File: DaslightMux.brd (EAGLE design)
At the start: 60 x 55.9 mm, 11 parts, among them U1 XC9572XL

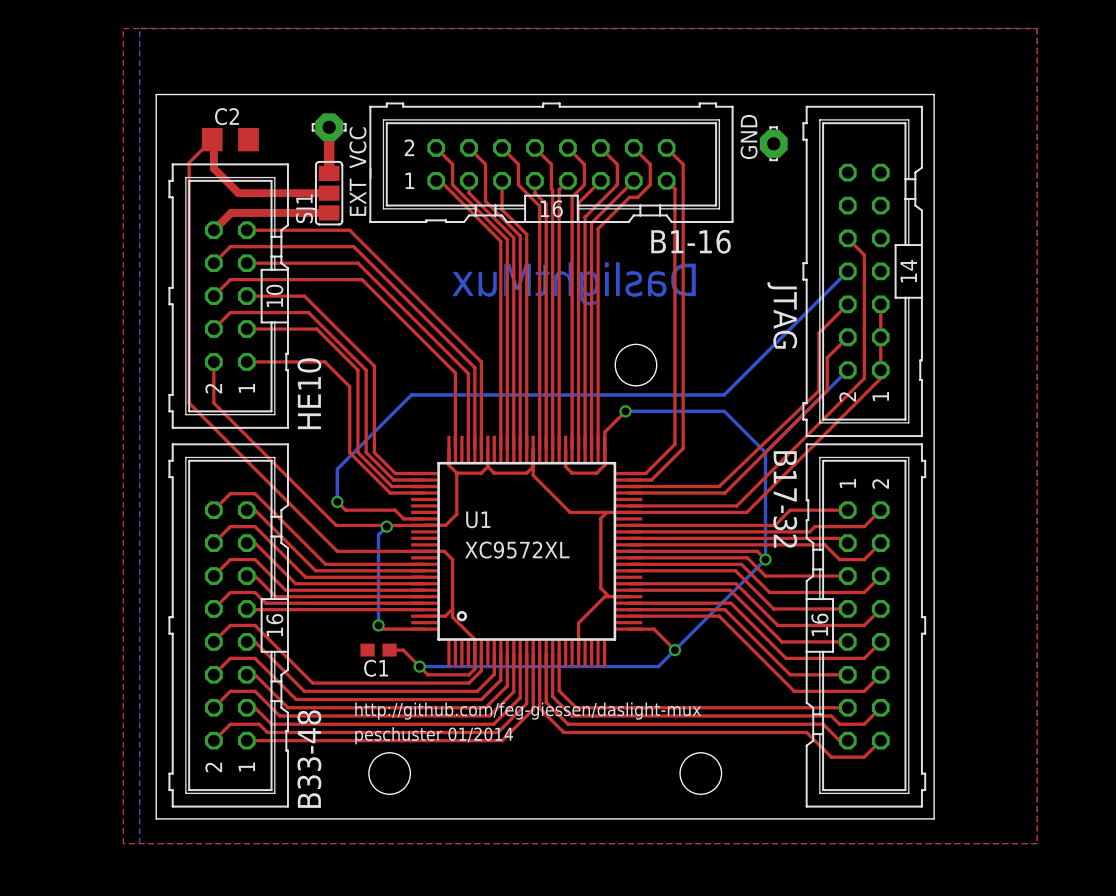
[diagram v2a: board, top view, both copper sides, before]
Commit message: Changed to SUB-D, therefore swapped "all" pins
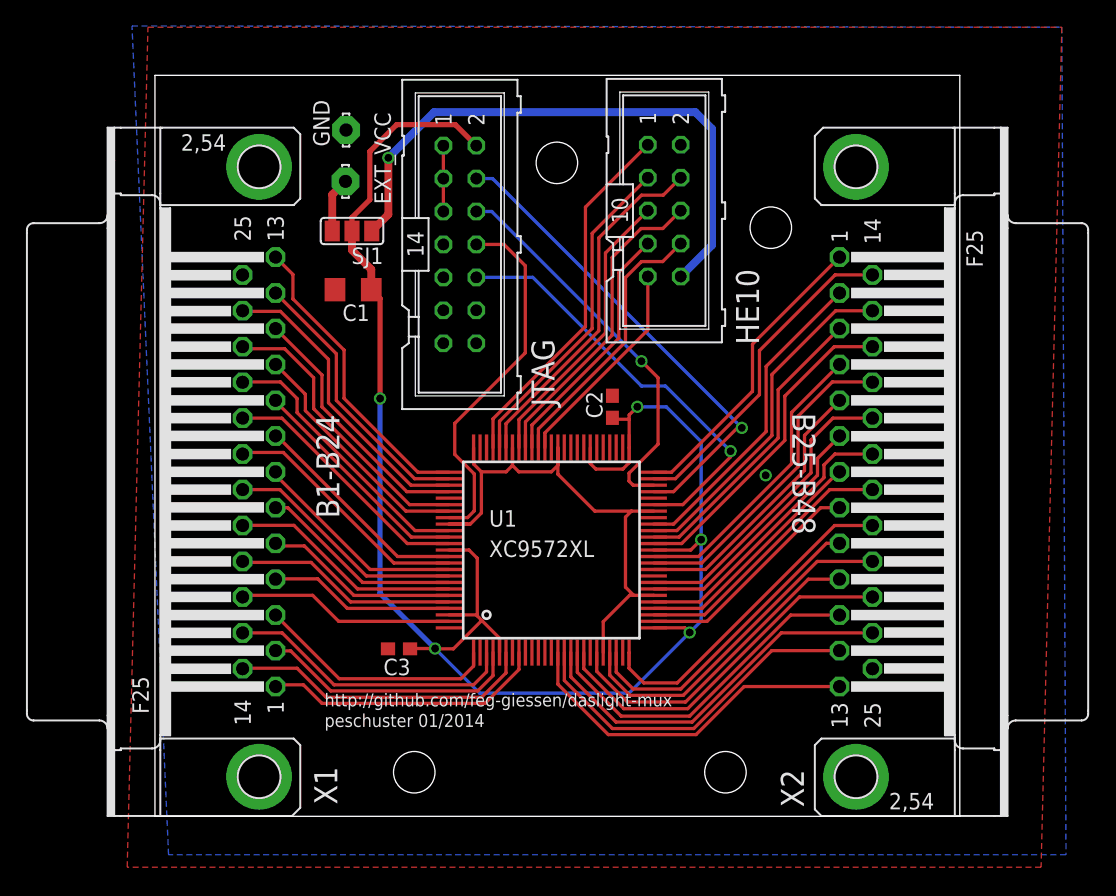
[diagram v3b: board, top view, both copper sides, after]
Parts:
- removed SV3: B1-16, con-harting-ml:ML16
- removed SV4: B17-32, con-harting-ml:ML16
- removed SV5: B33-48, con-harting-ml:ML16
- added C3: 100n, resistor:C0603
- added X1: B1-B24, con-subd:F25HP
- added X2: B25-B48, con-subd:F25HP
- C1: value 100n -> 10u; device resistor:C0603 -> resistor:C1206
- C2: value 10u -> 100n; device resistor:C1206 -> resistor:C0603
- SJ1: value (none) -> PWR_SEL
- moved C2 36.0 mm to (35.2, 31.8), turned to 90 degrees
- moved SV2 34.1 mm to (39.2, 46.9), turned to 270 degrees
- moved GND 33.0 mm to (14.6, 53.1)
- moved SV1 31.3 mm to (23.4, 44.3), turned to 270 degrees
- moved C1 27.9 mm to (15.2, 40.8)
- moved EXT_VCC 4.35 mm to (14.6, 49.2), turned to 270 degrees
- moved SJ1 3.41 mm to (15.1, 45.3), turned to 180 degrees
- moved U1 1.90 mm to (30.5, 20.7)
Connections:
- net B1: now also U1.8, X1.1; no longer SV3.1, U1.67
- net B10: now also U1.82, X1.10; no longer SV3.10, U1.56
- net B11: now also U1.79, X1.11; no longer SV3.11, U1.55
- net B12: now also U1.77, X1.12; no longer SV3.12, U1.54
- net B13: now also U1.76, X1.13; no longer SV3.13, U1.53
- net B14: now also U1.6, X1.14; no longer SV3.14, U1.52
- net B15: now also U1.3, X1.15; no longer SV3.15, U1.50
- net B16: now also U1.99, X1.16; no longer SV3.16, U1.49
- net B17: now also U1.96, X1.17; no longer SV4.1, U1.42
- net B18: now also U1.94, X1.18; no longer SV4.2, U1.41
- net B19: now also U1.92, X1.19; no longer SV4.3, U1.40
- net B2: now also U1.4, X1.2; no longer SV3.2, U1.66
- net B20: now also U1.90, X1.20; no longer SV4.4, U1.39
- net B21: now also U1.87, X1.21; no longer SV4.5, U1.37
- net B22: now also U1.85, X1.22; no longer SV4.6, U1.36
- net B23: now also U1.81, X1.23; no longer SV4.7, U1.35
- net B24: now also U1.78, X1.24; no longer SV4.8, U1.33
- net B25: now also U1.50, X2.1; no longer SV4.9, U1.32
- net B26: now also U1.42, X2.2; no longer SV4.10, U1.30
- net B27: now also U1.40, X2.3; no longer SV4.11, U1.29
- net B28: now also U1.37, X2.4; no longer SV4.12, U1.28
- net B29: now also U1.35, X2.5; no longer SV4.13, U1.18
- net B3: now also U1.1, X1.3; no longer SV3.3, U1.65
- net B30: now also U1.32, X2.6; no longer SV4.14, U1.17
- net B31: now also U1.29, X2.7; no longer SV4.15, U1.16
- net B32: now also U1.27, X2.8; no longer SV4.16, U1.15
- net B33: now also U1.23, X2.9; no longer SV5.1, U1.14
- net B34: now also U1.20, X2.10; no longer SV5.2, U1.13
- net B35: now also U1.17, X2.11; no longer SV5.3, U1.12
- net B36: now also U1.15, X2.12; no longer SV5.4, U1.11
- net B37: now also U1.14, X2.13; no longer SV5.5, U1.10
- net B38: now also U1.49, X2.14; no longer SV5.6, U1.9
- net B39: now also U1.41, X2.15; no longer SV5.7, U1.8
- net B4: now also U1.97, X1.4; no longer SV3.4, U1.64
- net B40: now also U1.39, X2.16; no longer SV5.8, U1.6
- net B41: now also U1.36, X2.17; no longer SV5.9, U1.97
- net B42: now also U1.33, X2.18; no longer SV5.10, U1.96
- net B43: now also U1.30, X2.19; no longer SV5.11, U1.95
- net B44: now also U1.28, X2.20; no longer SV5.12, U1.94
- net B45: now also U1.25, X2.21; no longer SV5.13, U1.93
- net B46: now also U1.22, X2.22; no longer SV5.14, U1.92
- net B47: now also U1.18, X2.23; no longer SV5.15, U1.91
- net B48: now also U1.16, X2.24; no longer SV5.16, U1.90
- net B5: now also U1.95, X1.5; no longer SV3.5, U1.63
- net B6: now also U1.93, X1.6; no longer SV3.6, U1.61
- net B7: now also U1.91, X1.7; no longer SV3.7, U1.60
- net B8: now also U1.89, X1.8; no longer SV3.8, U1.59
- net B9: now also U1.86, X1.9; no longer SV3.9, U1.58
- net GND: now also C3.2, X1.25, X2.25
- net O1: now also U1.64; no longer U1.70
- net O2: now also U1.65; no longer U1.71
- net O3: now also U1.66; no longer U1.72
- net O4: now also U1.67; no longer U1.74
- net O5: now also U1.68; no longer U1.76
- net O6: now also U1.70; no longer U1.77
- net O7: now also U1.71; no longer U1.78
- net O8: now also U1.72; no longer U1.79
- net VCC: now also C3.1
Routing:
- net GND: track 107.9 -> 48.6 mm, vias 2 -> 1
- net N$1: track 9.44 -> 45.5 mm, vias 0 -> 1
- net VCC: track 161.5 -> 131.9 mm, vias 4 -> 5
- net TDO: track 55.5 -> 28.4 mm, vias 1 -> 0
- net B32: track 32.6 -> 18.1 mm
- net TMS: track 23.3 -> 37.3 mm, vias 0 -> 1
- net B47: track 15.6 -> 28.4 mm
- net O1: track 29.0 -> 16.5 mm
- net B16: track 28.9 -> 16.8 mm
- net B41: track 13.7 -> 24.9 mm
- net B4: track 24.8 -> 14.3 mm
- net B45: track 15.0 -> 25.5 mm
- net B48: track 19.0 -> 29.4 mm
- net B30: track 30.0 -> 20.0 mm
- net O2: track 30.8 -> 21.2 mm
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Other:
- board size 60 x 55.9 mm -> 62.1 x 57.2 mm
- board text removed: "DaslightMux"

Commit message: Remodeled enclosure and adapted pcb layout
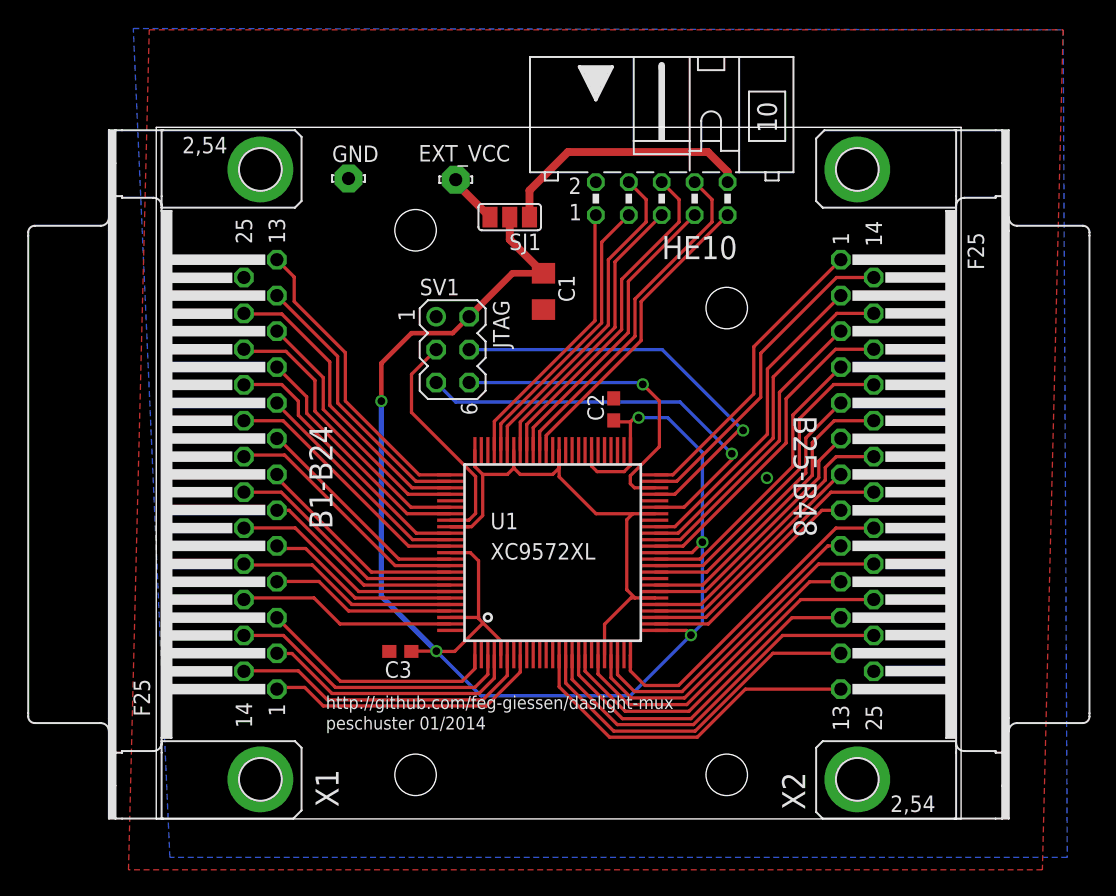
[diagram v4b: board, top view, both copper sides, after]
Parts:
- SV1: device con-harting-ml:ML14 -> con-lstb:MA03-2
- SV2: device con-harting-ml:ML10 -> con-harting-ml:ML10L
- moved C1 14.7 mm to (29.9, 40.7), turned to 270 degrees
- moved SJ1 12.2 mm to (27.3, 46.4)
- moved EXT_VCC 8.51 mm to (23.1, 49.3), turned to 0 degrees
- moved SV1 8.13 mm to (22.9, 36.2)
- moved GND 3.74 mm to (14.8, 49.4), turned to 0 degrees
- moved SV2 0.95 mm to (39.0, 47.8), turned to 0 degrees
- moved C2 0.22 mm to (35.3, 31.6)
- moved X2 0.22 mm to (54.1, 26.6)
- moved X1 0.22 mm to (8.03, 26.6)
- moved C3 0.22 mm to (18.8, 12.9)
- moved U1 0.22 mm to (30.6, 20.5)
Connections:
- net GND: no longer SV1.11, SV1.13, SV1.3, SV1.5, SV1.7, SV1.9
- net TDI: now also SV1.5; no longer SV1.10
- net TDO: now also SV1.3; no longer SV1.8
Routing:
- net N$1: track 45.5 -> 20.0 mm, vias 1 -> 0
- net TDO: track 28.4 -> 17.6 mm
- net VCC: track 131.9 -> 124.3 mm
- net O1: track 16.5 -> 23.9 mm
- net O8: track 28.3 -> 21.4 mm
- net TCK: track 30.3 -> 24.6 mm
- net O2: track 21.2 -> 26.7 mm
- net GND: track 48.6 -> 43.6 mm
- net TMS: track 37.3 -> 32.5 mm
- net O3: track 19.4 -> 23.3 mm
- net O7: track 25.6 -> 22.2 mm
- net O4: track 24.2 -> 26.1 mm
- net O6: track 27.4 -> 25.7 mm
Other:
- board size 62.1 x 57.2 mm -> 62.1 x 53.3 mm
